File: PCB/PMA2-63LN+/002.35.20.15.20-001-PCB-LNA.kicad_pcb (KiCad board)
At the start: 4 copper layers, 52.5 x 40.5 mm, 37 parts, among them U1 PMA2-63LN+, U2 PMA2-63LN+, U3 YAT-1A+, U4 L7805, U5 L7805

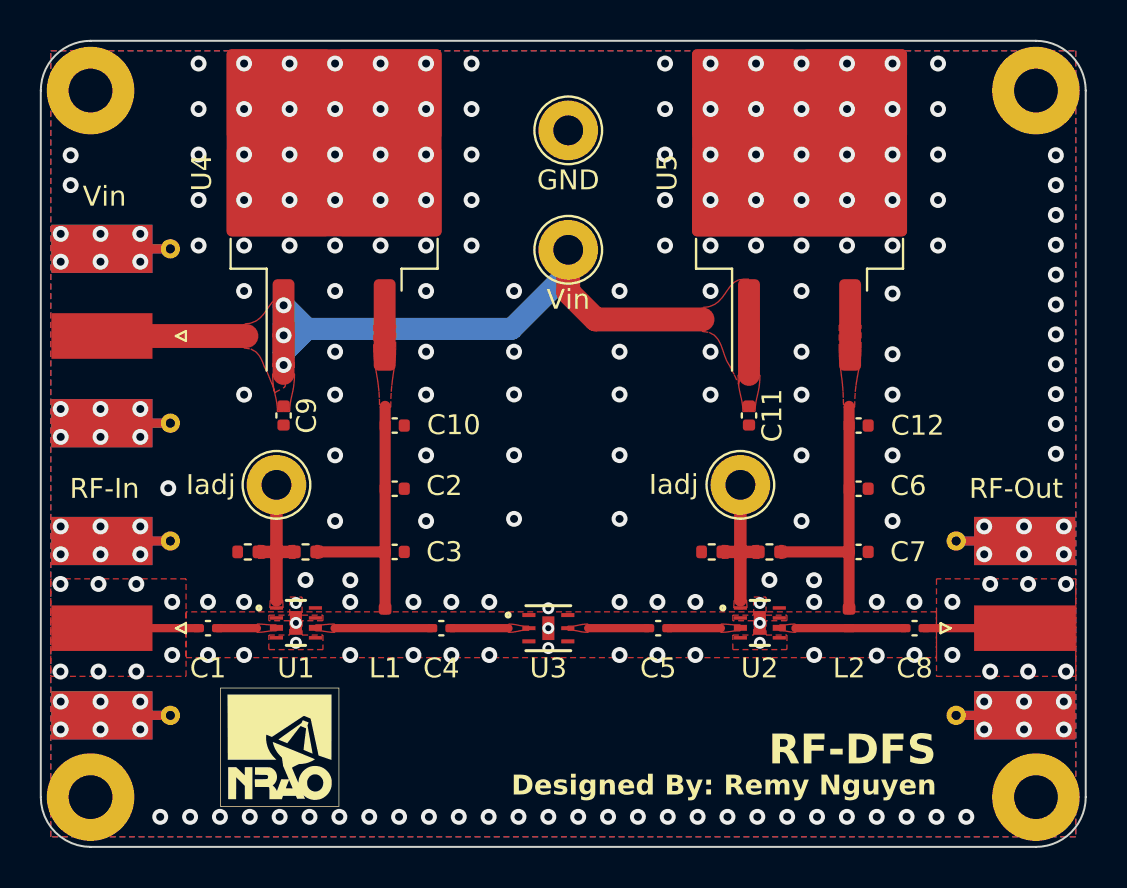
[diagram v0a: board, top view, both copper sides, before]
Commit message: pcb: added boms, updated readmes, changed silkscreen from dfs/ems to nmsm
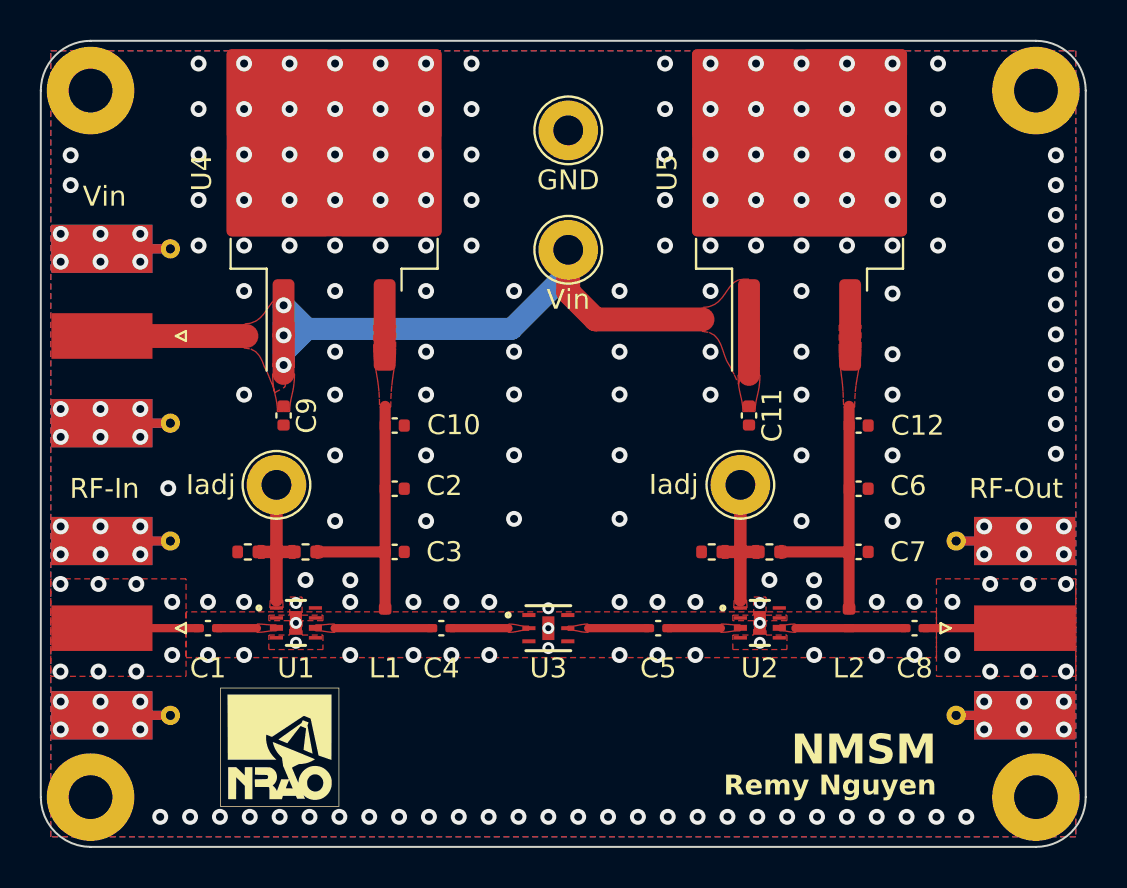
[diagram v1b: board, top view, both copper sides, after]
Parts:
- renumbered RF-In to J1, RF-Out to J2, Vin to J3, Iadj to TP1, Iadj to TP2, Vin to TP3, GND to TP4
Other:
- board text added: "NMSM"
- board text removed: "Designed By: Remy Nguyen"
- board text removed: "RF-DFS"
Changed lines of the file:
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@@
     (property "ki_keywords" "test point tp")
     (attr through_hole)
-    (fp_text reference "Vin" (at 0 2.5) (layer "F.SilkS")
+    (fp_text reference "TP3" (at 0 2.5) (layer "F.Fab")
         (effects (font (size 1 1) (thickness 0.15)))
     )
@@
         (effects (font (size 1 1) (thickness 0.15)))
     )
-    (fp_text user "${REFERENCE}" (at 0 2.5) (layer "F.Fab")
+    (fp_text user "Vin" (at 0 2.5) (layer "F.SilkS")
         (effects (font (size 1 1) (thickness 0.15)))
     )
@@
     (property "ki_keywords" "BNC SMA SMB SMC LEMO coaxial connector CINCH RCA")
     (attr smd)
-    (fp_text reference "RF-Out" (at -1.29 7.012) (layer "F.SilkS")
+    (fp_text reference "J2" (at -1.29 7.012) (layer "F.Fab")
         (effects (font (size 1 1) (thickness 0.15)))
     )
@@
         (effects (font (size 1 1) (thickness 0.15)))
     )
-    (fp_text user "${REFERENCE}" (at -1.29 7.012) (layer "F.Fab")
+    (fp_text user "RF-Out" (at -1.29 7.012) (layer "F.SilkS")
         (effects (font (size 1 1) (thickness 0.15)))
     )
@@
     (property "ki_keywords" "BNC SMA SMB SMC LEMO coaxial connector CINCH RCA")
     (attr smd)
-    (fp_text reference "RF-In" (at -1.59 -7.012) (layer "F.SilkS")
+    (fp_text reference "J1" (at -1.59 -7.012) (layer "F.Fab")
         (effects (font (size 1 1) (thickness 0.15)))
     )
@@
         (effects (font (size 1 1) (thickness 0.15)))
     )
-    (fp_text user "${REFERENCE}" (at -1.59 -7.012) (layer "F.Fab")
+    (fp_text user "RF-In" (at -1.59 -7.012) (layer "F.SilkS")
         (effects (font (size 1 1) (thickness 0.15)))
     )
@@
     (property "ki_keywords" "test point tp")
     (attr through_hole)
-    (fp_text reference "GND" (at 0 2.5) (layer "F.SilkS")
+    (fp_text reference "TP4" (at 0 2.5) (layer "F.Fab")
         (effects (font (size 1 1) (thickness 0.15)))
     )
@@
         (effects (font (size 1 1) (thickness 0.15)))
     )
-    (fp_text user "${REFERENCE}" (at 0 2.5) (layer "F.Fab")
+    (fp_text user "GND" (at 0 2.5) (layer "F.SilkS")
         (effects (font (size 1 1) (thickness 0.15)))
     )
@@
     (property "ki_keywords" "BNC SMA SMB SMC LEMO coaxial connector CINCH RCA")
     (attr smd)
-    (fp_text reference "Vin" (at -1.59 -7.012) (layer "F.SilkS")
+    (fp_text reference "J3" (at -1.59 -7.012) (layer "F.Fab")
         (effects (font (size 1 1) (thickness 0.15)))
     )
@@
         (effects (font (size 1 1) (thickness 0.15)))
     )
-    (fp_text user "${REFERENCE}" (at -1.59 -7.012) (layer "F.Fab")
+    (fp_text user "Vin" (at -1.59 -7.012) (layer "F.SilkS")
         (effects (font (size 1 1) (thickness 0.15)))
     )
@@
     (property "ki_keywords" "test point tp")
     (attr through_hole)
-    (fp_text reference "Iadj" (at -3.349 -0.01) (layer "F.SilkS")
+    (fp_text reference "TP2" (at -3.349 -0.01) (layer "F.Fab")
         (effects (font (size 1 1) (thickness 0.15)))
     )
@@
         (effects (font (size 1 1) (thickness 0.15)))
     )
-    (fp_text user "${REFERENCE}" (at -3.349 -0.01) (layer "F.Fab")
+    (fp_text user "Iadj" (at -3.349 -0.01) (layer "F.SilkS")
         (effects (font (size 1 1) (thickness 0.15)))
     )
@@
     (property "ki_keywords" "test point tp")
     (attr through_hole)
-    (fp_text reference "Iadj" (at -3.3 0) (layer "F.SilkS")
+    (fp_text reference "TP1" (at -3.3 0) (layer "F.Fab")
         (effects (font (size 1 1) (thickness 0.15)))
     )
@@
         (effects (font (size 1 1) (thickness 0.15)))
     )
-    (fp_text user "${REFERENCE}" (at -3.3 0) (layer "F.Fab")
+    (fp_text user "Iadj" (at -3.3 0) (layer "F.SilkS")
         (effects (font (size 1 1) (thickness 0.15)))
     )
@@
   (gr_line (start 132.222077 99.682077) (end 84.722077 99.682077)
     (stroke (width 0.1) (type default)) (layer "Edge.Cuts"))
-  (gr_text "RF-DFS" (at 127.222077 95.672077) (layer "F.SilkS")
+  (gr_text "NMSM" (at 127.222077 95.672077) (layer "F.SilkS")
     (effects (font (size 1.5 1.5) (thickness 0.3) bold) (justify right bottom))
   )
-  (gr_text "Designed By: Remy Nguyen" (at 127.222077 97.172077) (layer "F.SilkS")
+  (gr_text "Remy Nguyen" (at 127.222077 97.172077) (layer "F.SilkS")
     (effects (font (size 1 1) (thickness 0.2) bold) (justify right bottom))
   )

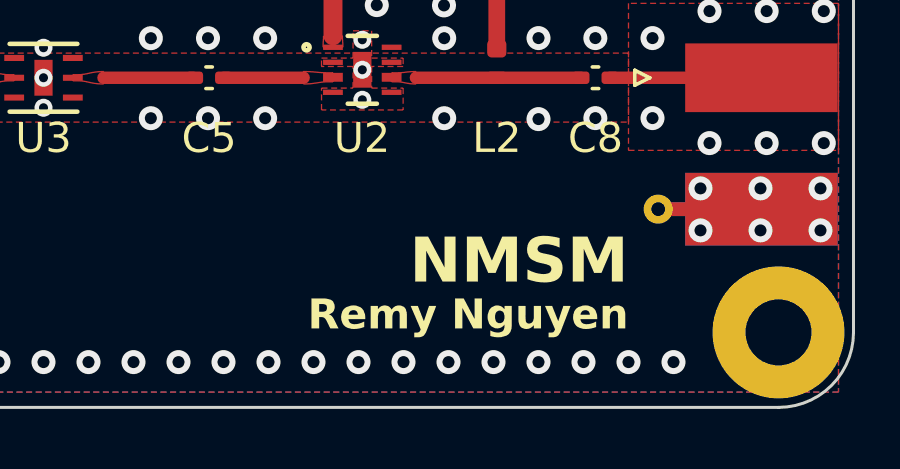
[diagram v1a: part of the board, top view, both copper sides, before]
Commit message: pcb: fixed silkscreen to be consistent with pma3-14ln+ (name, revision, device)
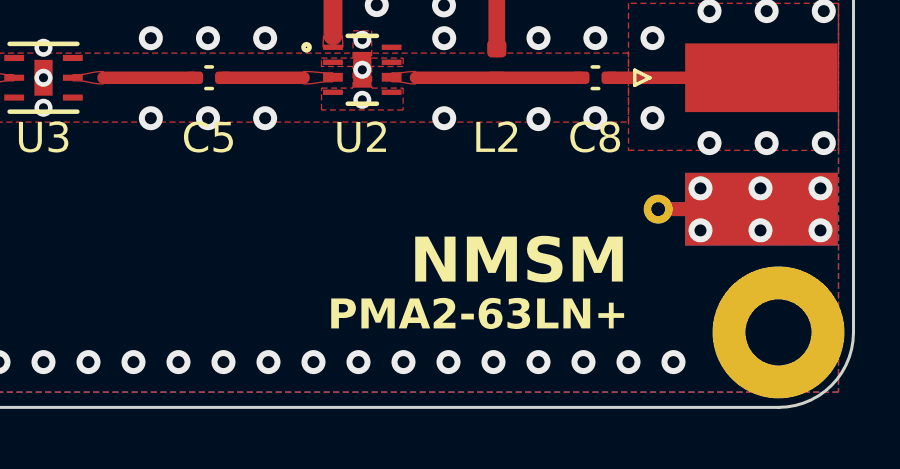
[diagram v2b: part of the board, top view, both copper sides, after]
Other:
- board text added: "PMA2-63LN+"
- board text added: "Rev B"
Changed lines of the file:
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@@
   (gr_line (start 132.222077 99.682077) (end 84.722077 99.682077)
     (stroke (width 0.1) (type default)) (layer "Edge.Cuts"))
+  (gr_text "Remy Nguyen" (at 127.22 97.17) (layer "B.SilkS")
+    (effects (font (size 1 1) (thickness 0.2) bold) (justify left bottom mirror))
+  )
+  (gr_text "Rev B" (at 91.3 97.17) (layer "B.SilkS")
+    (effects (font (size 1 1) (thickness 0.2) bold) (justify right bottom mirror))
+  )
   (gr_text "NMSM" (at 127.222077 95.672077) (layer "F.SilkS")
     (effects (font (size 1.5 1.5) (thickness 0.3) bold) (justify right bottom))
   )
-  (gr_text "Remy Nguyen" (at 127.222077 97.172077) (layer "F.SilkS")
+  (gr_text "PMA2-63LN+" (at 127.222077 97.172077) (layer "F.SilkS")
     (effects (font (size 1 1) (thickness 0.2) bold) (justify right bottom))
   )
